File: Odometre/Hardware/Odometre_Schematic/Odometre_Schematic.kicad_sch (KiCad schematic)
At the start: 20 parts, among them IC1 STM32C092FCP6, J1 Conn_01x03_Pin, J2 Conn_01x03_Pin, SW1 SW_Push, U1 MCP2562-E-SN, U2 LM1117DT-3.3

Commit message: modif
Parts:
- added J3: Conn_02x05_Odd_Even, symbol Connector_Generic:Conn_02x05_Odd_Even
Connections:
- net +3.3V: now also J3.2 (Pin_2)
- net DEBUG_SWCLK: now also J3.4 (Pin_4)
- net DEBUG_SWDIO: now also J3.3 (Pin_3)
- net GND: now also J3.1 (Pin_1), J3.5 (Pin_5), J3.9 (Pin_9)
- net NRST: now also J3.6 (Pin_6)
- net USART1_RX: now also J3.8 (Pin_8)
- net USART1_TX: now also J3.7 (Pin_7)
- no-connect marks 5 -> 6
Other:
- moved on the sheet: IC1

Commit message: modif
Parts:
- added J4: Conn_Laser, symbol Connector:Conn_01x03_Pin
- added J5: Conn_Alim, symbol Connector:Conn_01x02_Pin
- added R3: 120, symbol Device:R
- J3: value Conn_02x05_Odd_Even -> Conn_SWD
- R1, R2: value R -> 330
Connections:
- net +3.3V: now also J4.1 (Pin_1)
- net +5V: now also J5.1 (Pin_1)
- net CANH: now also R3.1
- net CANL: now also R3.2
- net GND: now also J4.3 (Pin_3), J5.2 (Pin_2)
- net TIM2_CH1: now also J4.2 (Pin_2)
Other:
- note added: "Connecteurs entrée"
- note removed: "Connecteurs entrée/sortie"

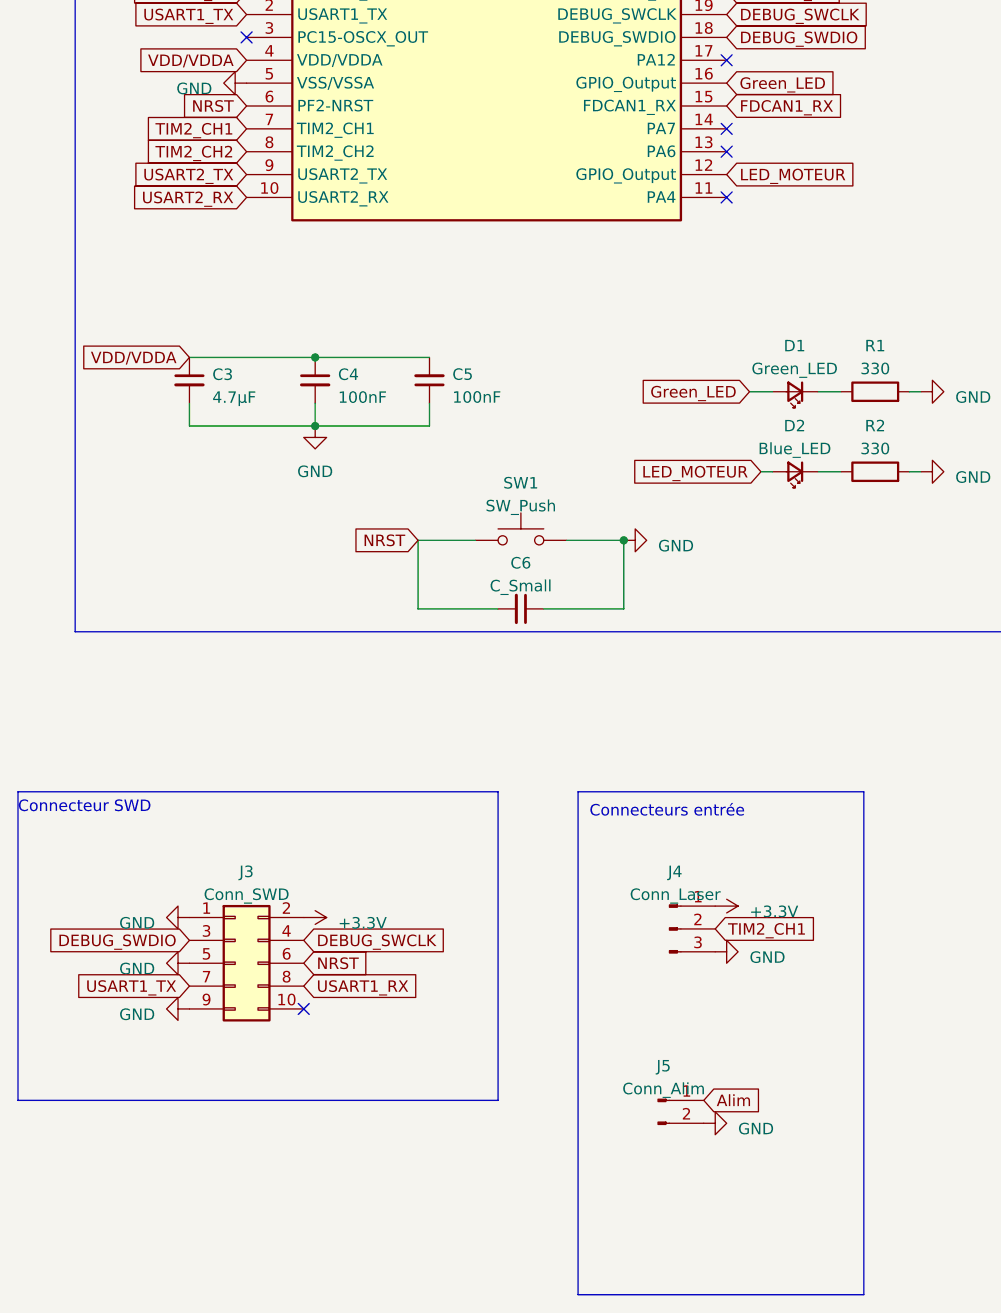
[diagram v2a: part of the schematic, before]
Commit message: modif du fichier ioc et du fiichier kicad
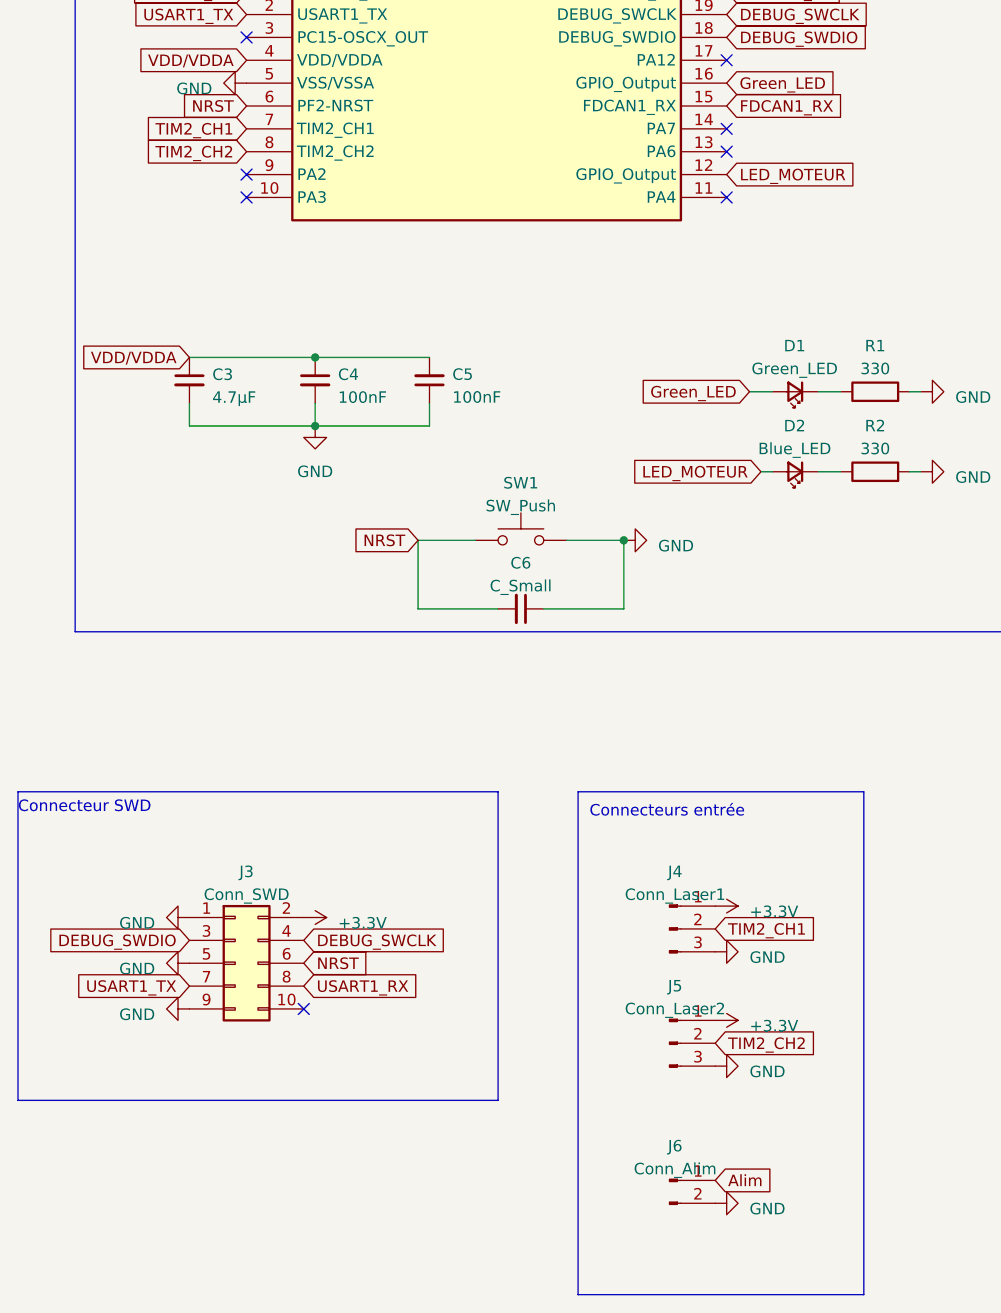
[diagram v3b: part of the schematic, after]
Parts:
- added J5: Conn_Laser2, symbol Connector:Conn_01x03_Pin
- J4: value Conn_Laser -> Conn_Laser1
- renumbered J5 to J6
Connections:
- net +3.3V: now also J5.1 (Pin_1)
- net GND: now also J5.3 (Pin_3)
- net TIM2_CH2: now also J5.2 (Pin_2)
- net USART2_RX: no longer names the net of IC1.10 (PA3)
- net USART2_TX: no longer names the net of IC1.9 (PA2)
- no-connect marks 6 -> 8
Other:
- moved on the sheet: J6
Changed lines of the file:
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@@
   (no_connect (at 93.98 64.77))
   (no_connect (at 93.98 59.69))
+  (no_connect (at 40.64 62.23))
   (no_connect (at 46.99 154.94))
   (no_connect (at 93.98 49.53))
+  (no_connect (at 40.64 64.77))
   (no_connect (at 40.64 46.99))
   (wire (pts (xy 255.27 45.72) (xy 262.89 45.72))
@@
     )
   )
-  (global_label "Alim" (shape input) (at 91.44 165.1 0) (fields_autoplaced)
-    (effects (font (size 1.27 1.27)) (justify left))
-    (property "Intersheetrefs" "${INTERSHEET_REFS}" (at 98.3977 165.1 0)
+  (global_label "Alim" (shape input) (at 92.71 173.99 0) (fields_autoplaced)
+    (effects (font (size 1.27 1.27)) (justify left))
+    (property "Intersheetrefs" "${INTERSHEET_REFS}" (at 99.6677 173.99 0)
       (effects (font (size 1.27 1.27)) (justify left) hide)
     )
@@
     )
   )
+  (global_label "TIM2_CH2" (shape input) (at 92.71 158.75 0) (fields_autoplaced)
+    (effects (font (size 1.27 1.27)) (justify left))
+    (property "Intersheetrefs" "${INTERSHEET_REFS}" (at 104.6267 158.75 0)
+      (effects (font (size 1.27 1.27)) (justify left) hide)
+    )
+  )
   (global_label "LED_MOTEUR" (shape input) (at 97.79 95.25 180) (fields_autoplaced)
     (effects (font (size 1.27 1.27)) (justify right))
@@
     )
   )
-  (global_label "USART2_TX" (shape input) (at 40.64 62.23 180) (fields_autoplaced)
-    (effects (font (size 1.27 1.27)) (justify right))
-    (property "Intersheetrefs" "${INTERSHEET_REFS}" (at 27.5138 62.23 0)
-      (effects (font (size 1.27 1.27)) (justify right) hide)
-    )
-  )
   (global_label "FDCAN1_TX" (shape input) (at 229.87 44.45 180) (fields_autoplaced)
     (effects (font (size 1.27 1.27)) (justify right))
@@
     (effects (font (size 1.27 1.27)) (justify right))
     (property "Intersheetrefs" "${INTERSHEET_REFS}" (at 21.7079 82.55 0)
-      (effects (font (size 1.27 1.27)) (justify right) hide)
-    )
-  )
-  (global_label "USART2_RX" (shape input) (at 40.64 64.77 180) (fields_autoplaced)
-    (effects (font (size 1.27 1.27)) (justify right))
-    (property "Intersheetrefs" "${INTERSHEET_REFS}" (at 27.2114 64.77 0)
       (effects (font (size 1.27 1.27)) (justify right) hide)
     )
@@
       (effects (font (size 1.27 1.27)))
     )
-    (property "Value" "Conn_Laser" (at 88.265 142.24 0)
+    (property "Value" "Conn_Laser1" (at 88.265 142.24 0)
       (effects (font (size 1.27 1.27)))
     )
@@
     )
   )
-  (symbol (lib_id "Connector:Conn_01x02_Pin") (at 86.36 165.1 0) (unit 1)
-    (in_bom yes) (on_board yes) (dnp no) (fields_autoplaced)
-    (property "Reference" "J5" (at 86.995 161.29 0)
-      (effects (font (size 1.27 1.27)))
-    )
-    (property "Value" "Conn_Alim" (at 86.995 163.83 0)
-      (effects (font (size 1.27 1.27)))
-    )
-    (property "Footprint" "" (at 86.36 165.1 0)
-      (effects (font (size 1.27 1.27)) hide)
-    )
-    (property "Datasheet" "~" (at 86.36 165.1 0)
+  (symbol (lib_id "power:+3.3V") (at 92.71 156.21 270) (unit 1)
+    (in_bom yes) (on_board yes) (dnp no) (fields_autoplaced)
+    (property "Reference" "#PWR020" (at 88.9 156.21 0)
+      (effects (font (size 1.27 1.27)) hide)
+    )
+    (property "Value" "+3.3V" (at 96.52 156.845 90)
+      (effects (font (size 1.27 1.27)) (justify left))
+    )
+    (property "Footprint" "" (at 92.71 156.21 0)
+      (effects (font (size 1.27 1.27)) hide)
+    )
+    (property "Datasheet" "" (at 92.71 156.21 0)
+      (effects (font (size 1.27 1.27)) hide)
+    )
+    (pin "1")
+    (instances
+      (project "Odometre_Schematic"
+        (path "/3741a7b9-879e-49a1-88bd-82d63456a983"
+          (reference "#PWR020") (unit 1)
+        )
+      )
+    )
+  )
+  (symbol (lib_id "Connector:Conn_01x02_Pin") (at 87.63 173.99 0) (unit 1)
+    (in_bom yes) (on_board yes) (dnp no) (fields_autoplaced)
+    (property "Reference" "J6" (at 88.265 170.18 0)
+      (effects (font (size 1.27 1.27)))
+    )
+    (property "Value" "Conn_Alim" (at 88.265 172.72 0)
+      (effects (font (size 1.27 1.27)))
+    )
+    (property "Footprint" "" (at 87.63 173.99 0)
+      (effects (font (size 1.27 1.27)) hide)
+    )
+    (property "Datasheet" "~" (at 87.63 173.99 0)
       (effects (font (size 1.27 1.27)) hide)
     )
@@
       (project "Odometre_Schematic"
         (path "/3741a7b9-879e-49a1-88bd-82d63456a983"
-          (reference "J5") (unit 1)
+          (reference "J6") (unit 1)
         )
       )
@@
     )
   )
+  (symbol (lib_id "Connector:Conn_01x03_Pin") (at 87.63 158.75 0) (unit 1)
+    (in_bom yes) (on_board yes) (dnp no) (fields_autoplaced)
+    (property "Reference" "J5" (at 88.265 152.4 0)
+      (effects (font (size 1.27 1.27)))
+    )
+    (property "Value" "Conn_Laser2" (at 88.265 154.94 0)
+      (effects (font (size 1.27 1.27)))
+    )
+    (property "Footprint" "" (at 87.63 158.75 0)
+      (effects (font (size 1.27 1.27)) hide)
+    )
+    (property "Datasheet" "~" (at 87.63 158.75 0)
+      (effects (font (size 1.27 1.27)) hide)
+    )
+    (pin "1")
+    (pin "2")
+    (pin "3")
+    (instances
+      (project "Odometre_Schematic"
+        (path "/3741a7b9-879e-49a1-88bd-82d63456a983"
+          (reference "J5") (unit 1)
+        )
+      )
+    )
+  )
   (symbol (lib_id "power:GND") (at 34.29 144.78 270) (unit 1)
     (in_bom yes) (on_board yes) (dnp no) (fields_autoplaced)
@@
     )
   )
-  (symbol (lib_id "power:GND") (at 91.44 167.64 90) (unit 1)
-    (in_bom yes) (on_board yes) (dnp no) (fields_autoplaced)
-    (property "Reference" "#PWR019" (at 97.79 167.64 0)
-      (effects (font (size 1.27 1.27)) hide)
-    )
-    (property "Value" "GND" (at 95.25 168.275 90)
+  (symbol (lib_id "power:GND") (at 92.71 176.53 90) (unit 1)
+    (in_bom yes) (on_board yes) (dnp no) (fields_autoplaced)
+    (property "Reference" "#PWR019" (at 99.06 176.53 0)
+      (effects (font (size 1.27 1.27)) hide)
+    )
+    (property "Value" "GND" (at 96.52 177.165 90)
       (effects (font (size 1.27 1.27)) (justify right))
     )
-    (property "Footprint" "" (at 91.44 167.64 0)
-      (effects (font (size 1.27 1.27)) hide)
-    )
-    (property "Datasheet" "" (at 91.44 167.64 0)
+    (property "Footprint" "" (at 92.71 176.53 0)
+      (effects (font (size 1.27 1.27)) hide)
+    )
+    (property "Datasheet" "" (at 92.71 176.53 0)
       (effects (font (size 1.27 1.27)) hide)
     )
@@
         )
       )
+    )
+  )
+  (symbol (lib_id "power:GND") (at 92.71 161.29 90) (unit 1)
+    (in_bom yes) (on_board yes) (dnp no) (fields_autoplaced)
+    (property "Reference" "#PWR021" (at 99.06 161.29 0)
+      (effects (font (size 1.27 1.27)) hide)
+    )
+    (property "Value" "GND" (at 96.52 161.925 90)
+      (effects (font (size 1.27 1.27)) (justify right))
+    )
+    (property "Footprint" "" (at 92.71 161.29 0)
+      (effects (font (size 1.27 1.27)) hide)
+    )
+    (property "Datasheet" "" (at 92.71 161.29 0)
+      (effects (font (size 1.27 1.27)) hide)
+    )
+    (pin "1")
+    (instances
+      (project "Odometre_Schematic"
+        (path "/3741a7b9-879e-49a1-88bd-82d63456a983"
+          (reference "#PWR021") (unit 1)
+        )
+      )

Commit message: Changement d'assocation
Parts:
- R3: footprint (none) -> Resistor_SMD:R_0603_1608Metric_Pad0.98x0.95mm_HandSolder
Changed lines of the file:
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@@
       (effects (font (size 1.27 1.27)) (justify left))
     )
-    (property "Footprint" "" (at 261.112 49.53 90)
+    (property "Footprint" "Resistor_SMD:R_0603_1608Metric_Pad0.98x0.95mm_HandSolder" (at 261.112 49.53 90)
       (effects (font (size 1.27 1.27)) hide)
     )

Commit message: modif kicad
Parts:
- removed J3: Conn_SWD, symbol Connector_Generic:Conn_02x05_Odd_Even
- removed J6: Conn_Alim, symbol Connector:Conn_01x02_Pin
- added J3: Conn_Alim, symbol Connector:Conn_01x03_Pin
- added J7: Conn_02x04_Odd_Even, symbol Connector_Generic:Conn_02x04_Odd_Even
- added SW2: SW_SPST, symbol Switch:SW_SPST
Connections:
- net +3.3V: now also J7.2 (Pin_2)
- net +5V: now also J3.1 (Pin_1)
- net DEBUG_SWCLK: now also J7.4 (Pin_4)
- net DEBUG_SWDIO: now also J7.3 (Pin_3)
- net GND: now also J3.2 (Pin_2), J7.1 (Pin_1), J7.5 (Pin_5), SW2.2 (B)
- net NRST: now also J7.6 (Pin_6)
- net USART1_RX: now also J7.8 (Pin_8)
- net USART1_TX: now also J7.7 (Pin_7)
- new net SWITCH: J3.3 (Pin_3), SW2.1 (A)
- no-connect marks 8 -> 7

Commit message: modif
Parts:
- removed J7: Conn_02x04_Odd_Even, symbol Connector_Generic:Conn_02x04_Odd_Even
- added J6: Conn_02x05_Odd_Even, symbol Connector_Generic:Conn_02x05_Odd_Even
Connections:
- net +3.3V: now also J6.2 (Pin_2)
- net DEBUG_SWCLK: now also J6.4 (Pin_4)
- net DEBUG_SWDIO: now also J6.3 (Pin_3)
- net GND: now also J1.2 (Pin_2), J2.2 (Pin_2), J6.1 (Pin_1), J6.5 (Pin_5), J6.9 (Pin_9)
- net NRST: now also J6.6 (Pin_6)
- net USART1_RX: now also J6.8 (Pin_8)
- net USART1_TX: now also J6.7 (Pin_7)
- no-connect marks 7 -> 8

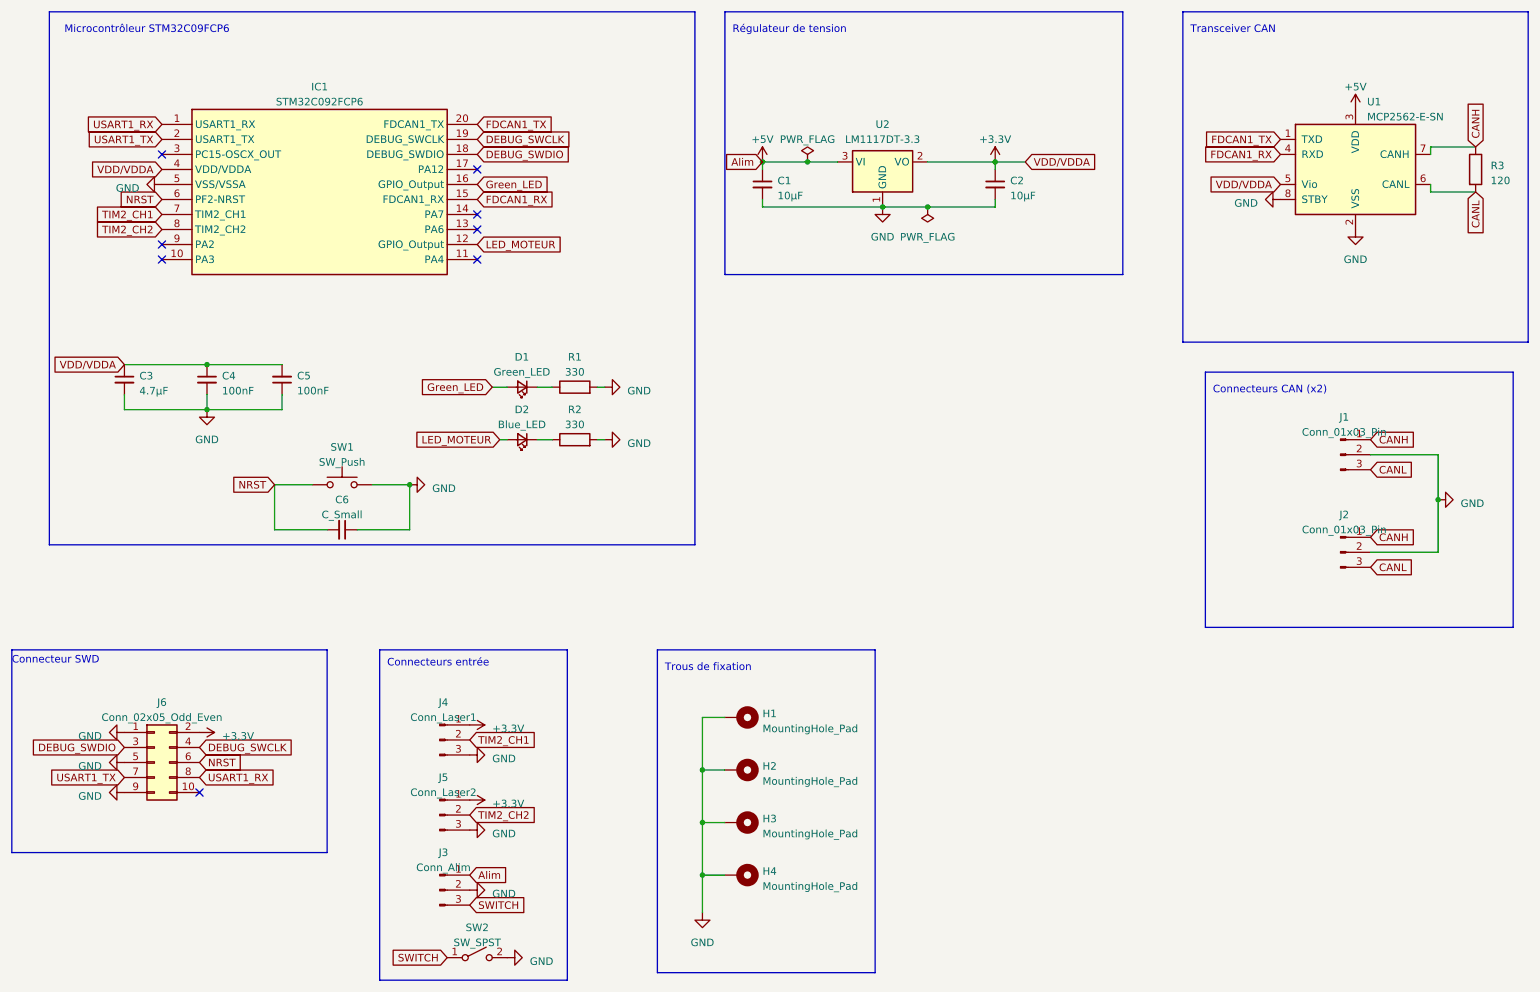
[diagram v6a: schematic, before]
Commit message: changement de connecteur
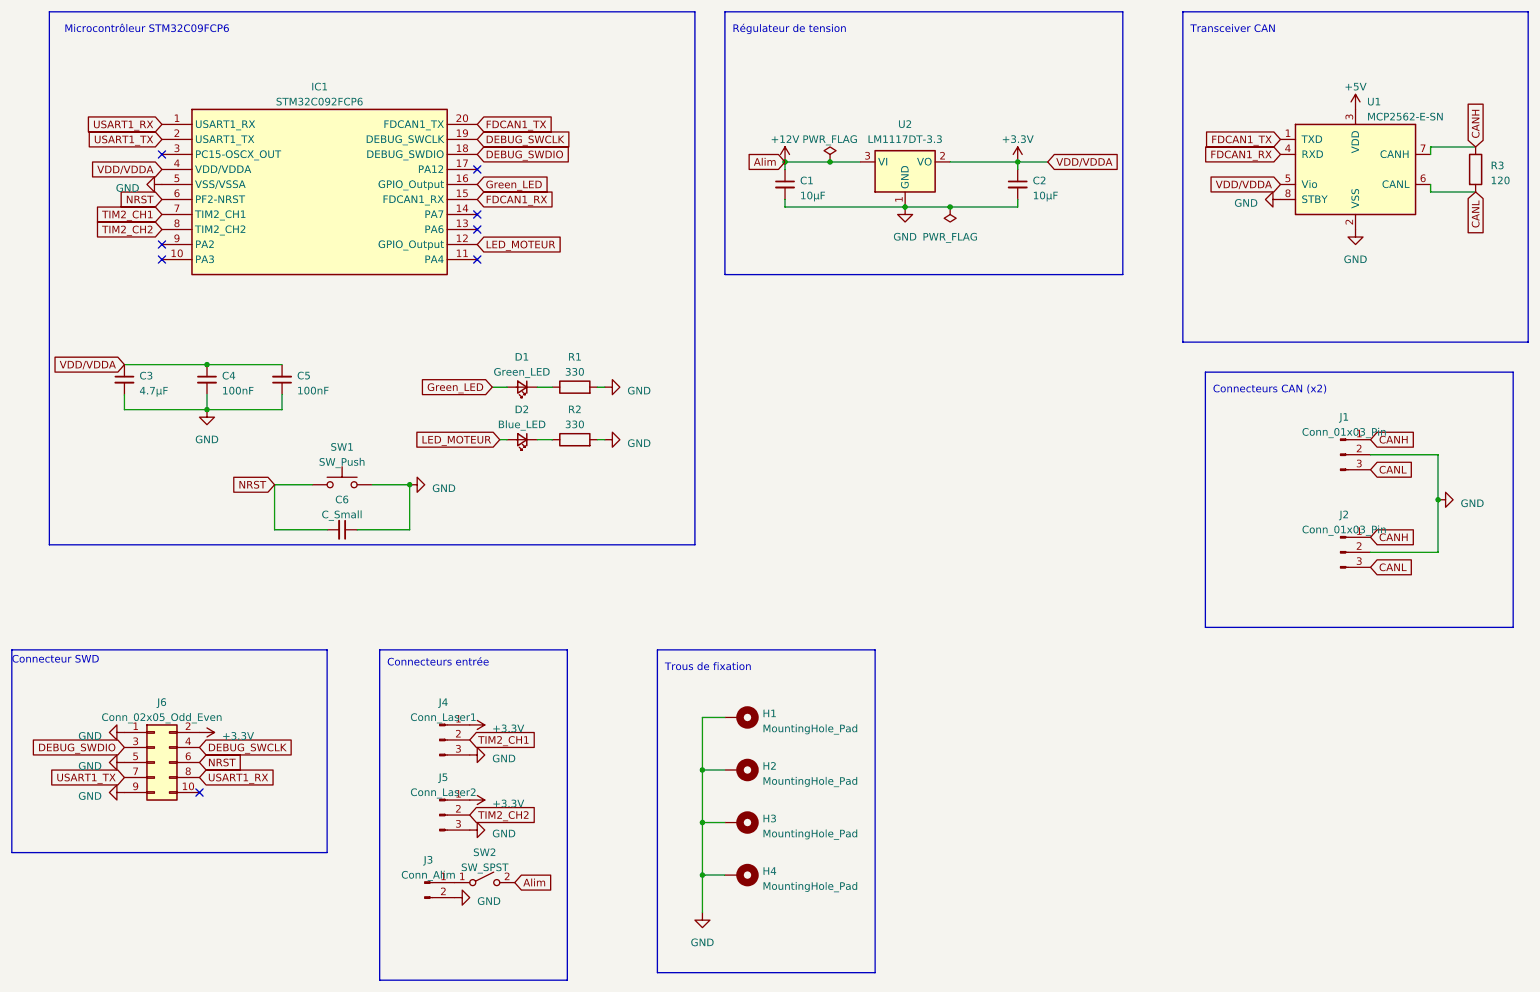
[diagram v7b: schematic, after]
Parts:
- removed J3: Conn_Alim, symbol Connector:Conn_01x03_Pin
- added J3: Conn_Alim, symbol Connector:Conn_01x02_Pin
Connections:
- net +5V: no longer C1.1, U2.3 (VI)
- net GND: now also J3.2 (Pin_2); no longer SW2.2 (B)
- net SWITCH: no longer names the net of SW2.1 (A)
- net SWITCH: now also J3.1 (Pin_1)
- new net +12V: C1.1, SW2.2 (B), U2.3 (VI)
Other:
- moved on the sheet: C1, C2, SW2, U2
